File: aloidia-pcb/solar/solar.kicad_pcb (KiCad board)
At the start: 2 copper layers, 132 x 13.8 mm, 6 parts, among them J1 S2B-PH-SM4-TB(LF)(SN)

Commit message: Added solar breakout module physical footprint
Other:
- board text added: "91.7"
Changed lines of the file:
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@@
   (gr_line (start 222.8 91.95) (end 219.85 91.95) (layer "Cmts.User") (width 0.08))
   (gr_line (start 222.8 78.05) (end 219.8 78.05) (layer "Cmts.User") (width 0.08))
+  (gr_line (start 87.8 76.6) (end 88.6 75.8) (layer "Cmts.User") (width 0.15))
+  (gr_line (start 87.8 76.6) (end 88.6 77.4) (layer "Cmts.User") (width 0.15))
+  (gr_line (start 179.5 76.6) (end 178.7 77.4) (layer "Cmts.User") (width 0.15))
   (gr_line (start 221.8 91.9) (end 222.6 91.1) (layer "Cmts.User") (width 0.15))
+  (gr_line (start 179.55 78.1) (end 179.55 75.05) (layer "Cmts.User") (width 0.08))
   (gr_line (start 221.8 78.1) (end 221 78.9) (layer "Cmts.User") (width 0.15))
   (gr_line (start 87.8 93.9) (end 88.6 93.1) (layer "Cmts.User") (width 0.15))
@@
   (gr_line (start 219.85 95) (end 219.85 91.95) (layer "Cmts.User") (width 0.08))
   (gr_line (start 219.8 93.9) (end 219 94.7) (layer "Cmts.User") (width 0.15))
+  (gr_line (start 87.75 78.1) (end 87.75 75.1) (layer "Cmts.User") (width 0.08))
+  (gr_line (start 179.5 76.6) (end 87.8 76.6) (layer "Cmts.User") (width 0.15))
   (gr_line (start 87.8 93.9) (end 219.8 93.9) (layer "Cmts.User") (width 0.15))
   (gr_line (start 221.8 78.1) (end 222.6 78.9) (layer "Cmts.User") (width 0.15))
   (gr_line (start 221.8 91.9) (end 221.8 78.1) (layer "Cmts.User") (width 0.15))
+  (gr_line (start 179.5 76.6) (end 178.7 75.8) (layer "Cmts.User") (width 0.15))
   (gr_line (start 219.8 93.9) (end 219 93.1) (layer "Cmts.User") (width 0.15))
   (gr_line (start 87.75 94.9) (end 87.75 91.9) (layer "Cmts.User") (width 0.08))
@@
   (gr_line (start 87.8 78.1) (end 93.1 78.1) (layer "Edge.Cuts") (width 0.1))
   (gr_line (start 93.1 91.9) (end 95.6 89.4) (layer "Edge.Cuts") (width 0.1))
+  (gr_text "91.7" (at 132.05 75.5) (layer "Cmts.User")
+    (effects (font (size 1 1) (thickness 0.15)))
+  )
   (gr_text "13.8" (at 224.1 85) (layer "Cmts.User")
     (effects (font (size 1 1) (thickness 0.15)))

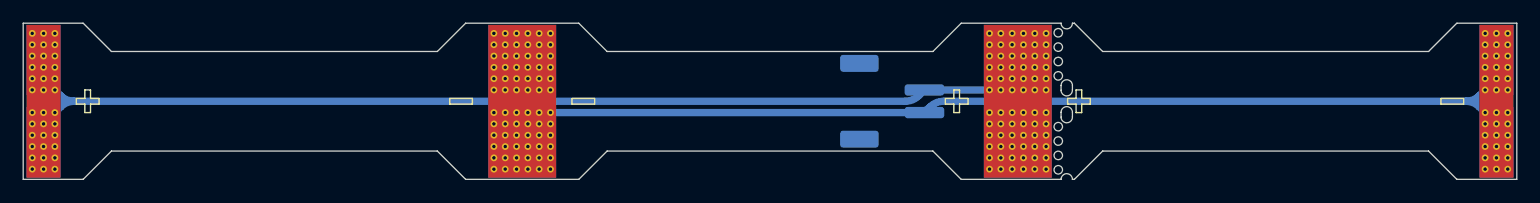
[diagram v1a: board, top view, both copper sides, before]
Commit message: Changed connectors to jst-sh
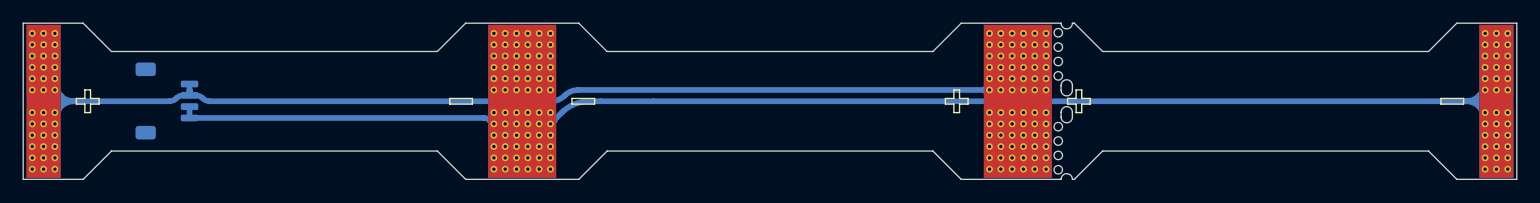
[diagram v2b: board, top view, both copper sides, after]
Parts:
- J1: value S2B-PH-SM4-TB(LF)(SN) -> SM04B-SRSS-TB(LF)(SN); footprint Connector_JST:JST_PH_S2B-PH-SM4-TB_1x02-1MP_P2.00mm_Horizontal -> Connector_JST:JST_SH_SM04B-SRSS-TB_1x04-1MP_P1.00mm_Horizontal
- moved J1 64.1 mm to (100.5, 85.0)
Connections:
- J1 pad 2: /CELL+ -> /CELL-
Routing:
- net /CELL-: track 86.3 -> 114.8 mm
- net /CELL+: track 86.4 -> 88.5 mm
